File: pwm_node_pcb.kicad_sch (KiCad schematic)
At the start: 42 parts, among them J1 CAN1, J2 TC2050-IDC-NL, J3 Battery, J5 Load Source, J6 5V Breakout, U1 LMR51430, U2 TJA1051T/3, U3 LD1117S33CTR, U4 STM32L432KCU, U5 TXB0104QPWRQ1, Y1 ECS-2520MV-080-BN

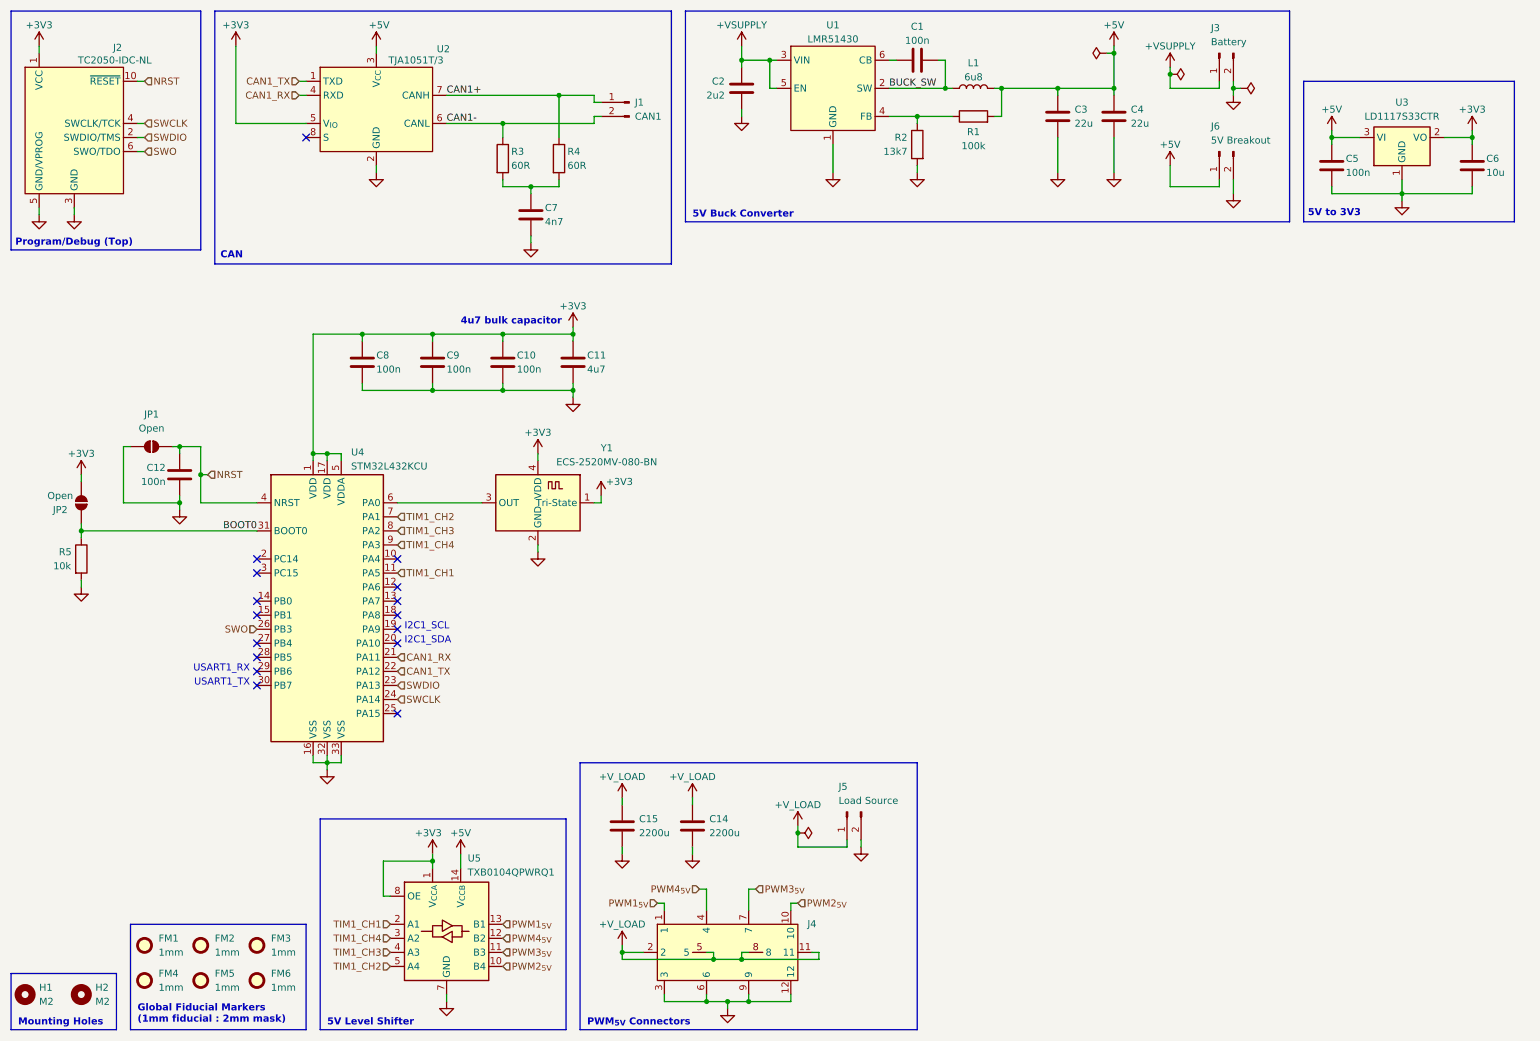
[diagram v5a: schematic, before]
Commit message: Add minor decoupling caps, board cleanup
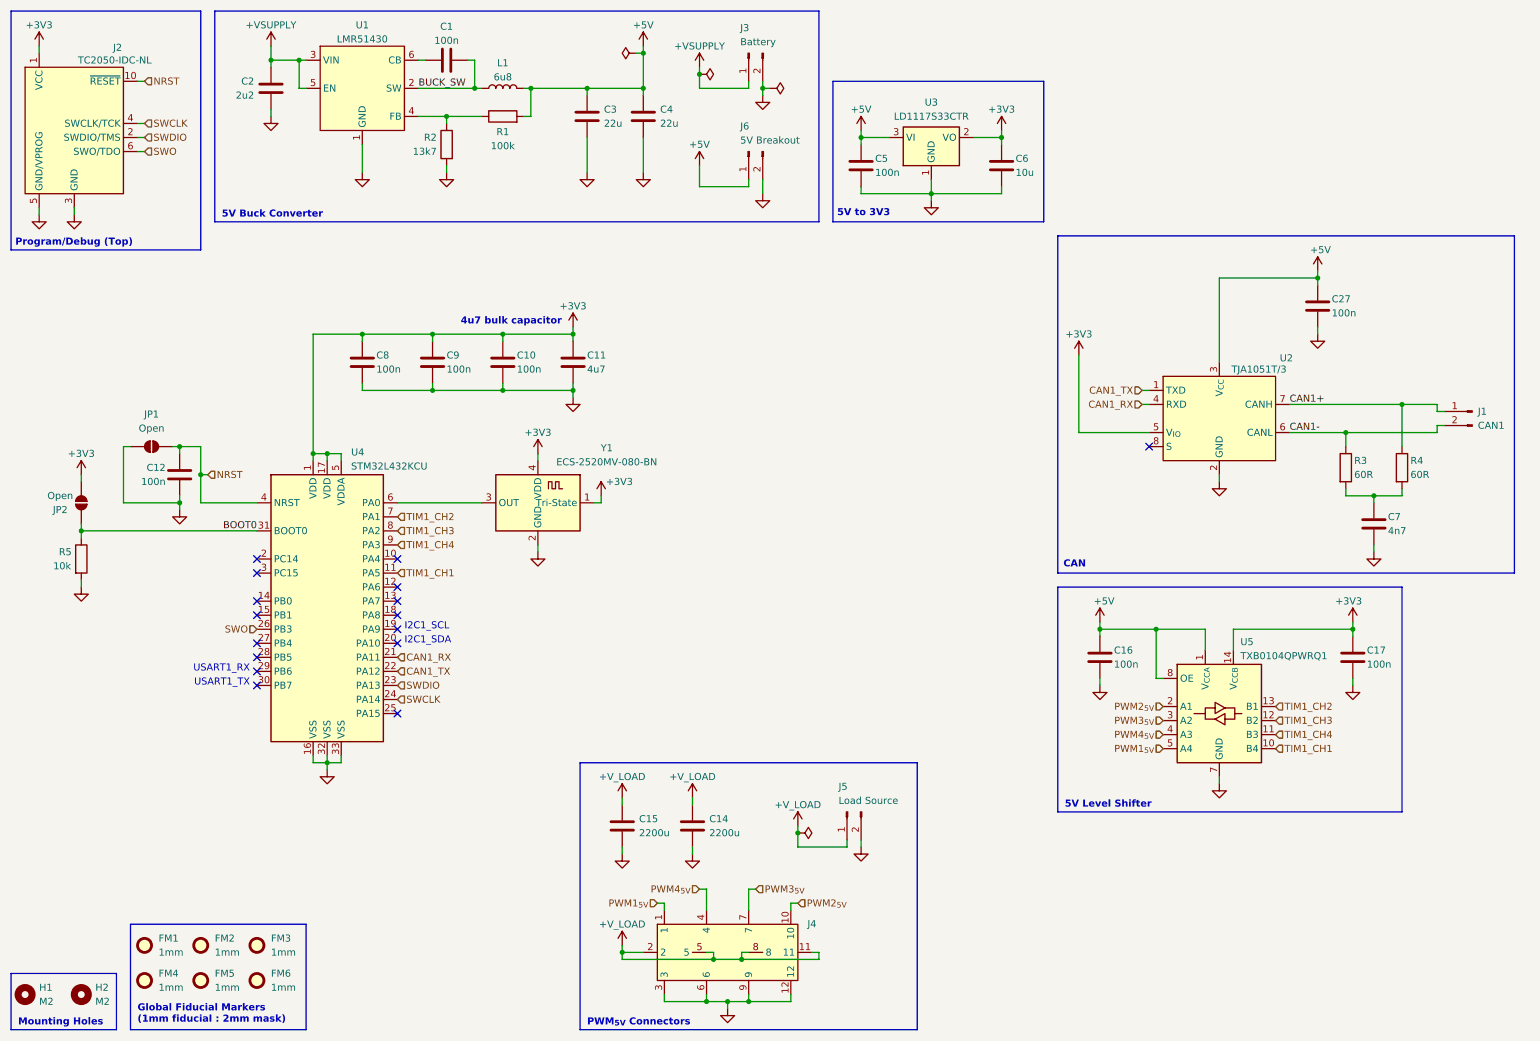
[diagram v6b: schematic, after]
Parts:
- added C16, C17, C27: 100n, Capacitor_SMD:C_0603_1608Metric, symbol Device:C
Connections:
- net +3V3: now also U5.14 (V_{CCB}), C17.1; no longer U5.1 (V_{CCA}), U5.8 (OE)
- net +5V: now also U5.1 (V_{CCA}), U5.8 (OE), C16.1, C27.1; no longer U5.14 (V_{CCB})
- net GND: now also C16.2, C17.2, C27.2
- net PWM1_{5V}: now also U5.5 (A4); no longer U5.13 (B1)
- net PWM2_{5V}: now also U5.2 (A1); no longer U5.10 (B4)
- net PWM3_{5V}: now also U5.3 (A2); no longer U5.11 (B3)
- net PWM4_{5V}: now also U5.4 (A3); no longer U5.12 (B2)
- net TIM1_CH1: now also U5.10 (B4); no longer U5.2 (A1)
- net TIM1_CH2: now also U5.13 (B1); no longer U5.5 (A4)
- net TIM1_CH3: now also U5.12 (B2); no longer U5.4 (A3)
- net TIM1_CH4: now also U5.11 (B3); no longer U5.3 (A2)
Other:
- moved on the sheet: C1, C2, C3, C4, C5, C6, C7, J1, J3, J6, L1, R1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

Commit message: Add TVS and schottky diodes
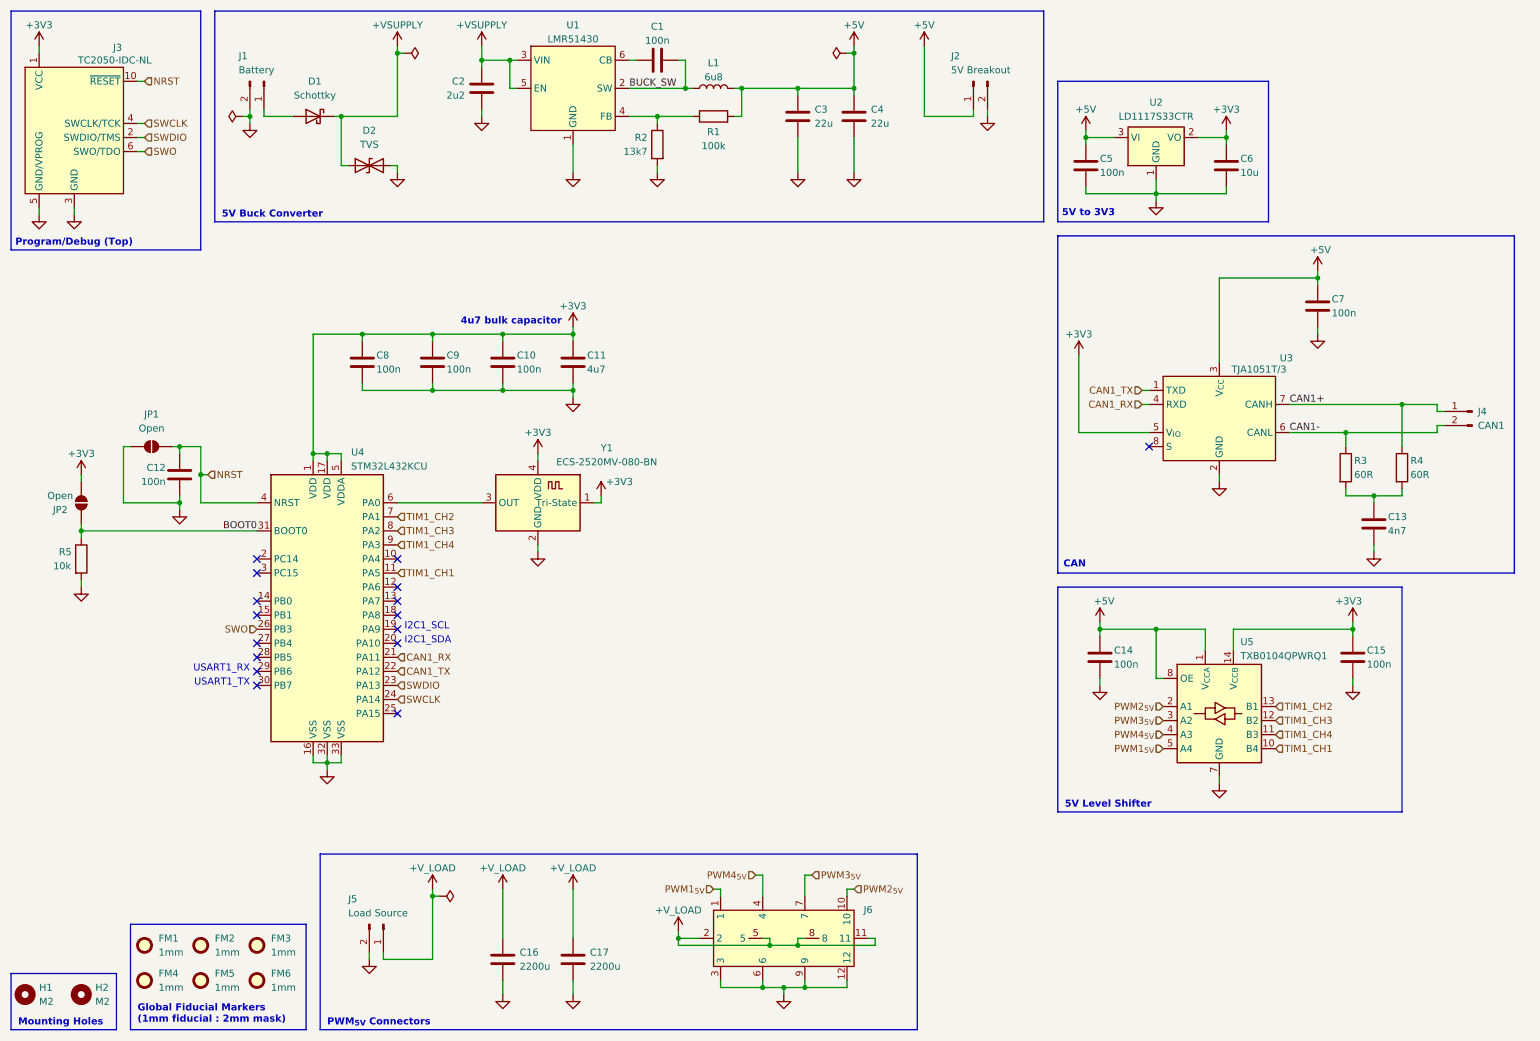
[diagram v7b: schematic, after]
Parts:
- added D1: Schottky, Diode_SMD:D_SMA, symbol Device:D_Schottky
- added D2: TVS, Diode_SMD:D_SMA, symbol Device:D_TVS
- renumbered C7 to C13, C16 to C14, C17 to C15, C15 to C16, C14 to C17, C27 to C7, J3 to J1, J6 to J2, J2 to J3, J1 to J4, J4 to J6, U3 to U2, U2 to U3
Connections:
- net +VSUPPLY: now also D1.1 (K), D2.1 (A1); no longer J1.1 (Pin_1)
- net GND: now also D2.2 (A2)
- new net: D1.2 (A), J1.1 (Pin_1)
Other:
- moved on the sheet: C1, C16, C17, C2, C3, C4, C5, C6, J1, J2, J5, J6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

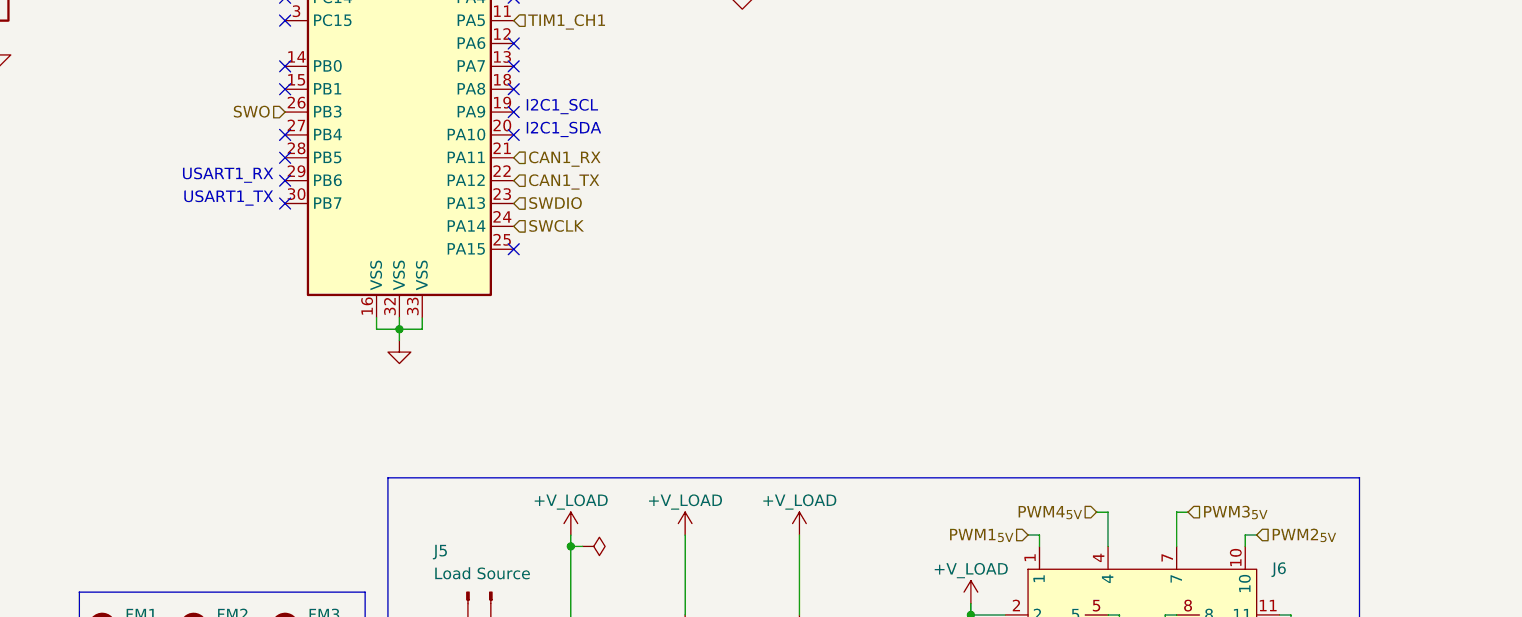
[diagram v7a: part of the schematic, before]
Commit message: Add testpads/UART breakout
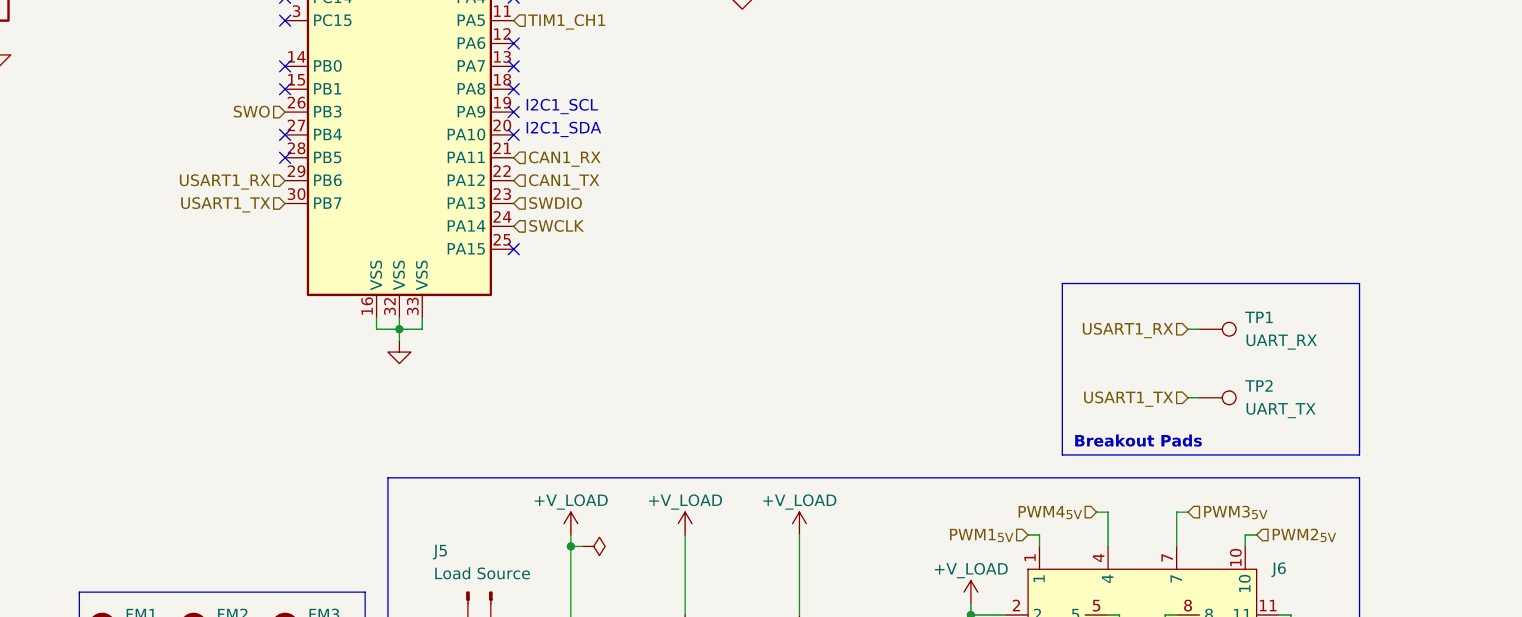
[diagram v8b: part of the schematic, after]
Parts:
- added TP1: UART_RX, TestPoint:TestPoint_Pad_D1.5mm, symbol Connector:TestPoint
- added TP2: UART_TX, TestPoint:TestPoint_Pad_D1.5mm, symbol Connector:TestPoint
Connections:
- net USART1_RX: now reaches U4.29 (PB6)
- net USART1_RX: now also TP1.1
- net USART1_TX: now reaches U4.30 (PB7)
- net USART1_TX: now also TP2.1
- no-connect marks 16 -> 14
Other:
- note added: "Breakout Pads"
- note removed: "USART1_RX"
- note removed: "USART1_TX"
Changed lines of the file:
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@@
 	)
 	(rectangle
+		(start 143.51 143.51)
+		(end 176.53 162.56)
+		(stroke
+			(width 0)
+			(type default)
+		)
+		(fill
+			(type none)
+		)
+	)
+	(rectangle
 		(start 34.29 177.8)
 		(end 66.04 196.85)
@@
 		)
 	)
-	(text "USART1_TX"
-		(exclude_from_sim no)
-		(at 55.88 134.112 0)
-		(effects
-			(font
-				(size 1.27 1.27)
-			)
-			(justify right)
-		)
-	)
 	(text "I2C1_SCL"
 		(exclude_from_sim no)
@@
 		)
 	)
-	(text "Global Fiducial Markers\n(1mm fiducial : 2mm mask)"
+	(text "I2C1_SDA"
 		(exclude_from_sim no)
-		(at 35.56 192.278 0)
+		(at 83.82 126.492 0)
+		(effects
+			(font
+				(size 1.27 1.27)
+			)
+			(justify left)
+		)
+	)
+	(text "Breakout Pads"
+		(exclude_from_sim no)
+		(at 144.78 160.528 0)
 		(effects
 			(font
@@
 		)
 	)
-	(text "Program/Debug (Top)"
+	(text "Global Fiducial Markers\n(1mm fiducial : 2mm mask)"
 		(exclude_from_sim no)
-		(at 13.462 53.848 0)
+		(at 35.56 192.278 0)
 		(effects
 			(font
@@
 		)
 	)
-	(text "I2C1_SDA"
+	(text "Program/Debug (Top)"
 		(exclude_from_sim no)
-		(at 83.82 126.492 0)
+		(at 13.462 53.848 0)
 		(effects
 			(font
 				(size 1.27 1.27)
+				(bold yes)
 			)
-			(justify left)
+			(justify left top)
 		)
 	)
@@
 		)
 	)
-	(text "USART1_RX"
-		(exclude_from_sim no)
-		(at 55.88 131.572 0)
-		(effects
-			(font
-				(size 1.27 1.27)
-			)
-			(justify right)
-		)
-	)
 	(junction
 		(at 232.41 35.56)
@@
 	)
 	(no_connect
+		(at 82.55 124.46)
+	)
+	(no_connect
 		(at 82.55 116.84)
 	)
@@
 	)
 	(no_connect
-		(at 57.15 114.3)
+		(at 82.55 127)
 	)
 	(no_connect
-		(at 82.55 127)
+		(at 57.15 114.3)
 	)
 	(no_connect
@@
 	)
 	(no_connect
-		(at 57.15 132.08)
-	)
-	(no_connect
 		(at 218.44 91.44)
 	)
 	(no_connect
-		(at 82.55 124.46)
-	)
-	(no_connect
 		(at 57.15 111.76)
 	)
@@
 		(at 57.15 129.54)
 	)
-	(no_connect
-		(at 57.15 134.62)
-	)
 	(wire
 		(pts
@@
 	(wire
 		(pts
+			(xy 157.48 156.21) (xy 158.75 156.21)
+		)
+		(stroke
+			(width 0)
+			(type default)
+		)
+	)
+	(wire
+		(pts
 			(xy 129.54 31.75) (xy 129.54 33.02)
 		)
@@
 	(wire
 		(pts
+			(xy 157.48 148.59) (xy 158.75 148.59)
+		)
+		(stroke
+			(width 0)
+			(type default)
+		)
+	)
+	(wire
+		(pts
 			(xy 80.01 184.15) (xy 80.01 182.88)
 		)
@@
 		)
 	)
+	(hierarchical_label "USART1_TX"
+		(shape input)
+		(at 157.48 156.21 180)
+		(effects
+			(font
+				(size 1.27 1.27)
+			)
+			(justify right)
+		)
+	)
 	(hierarchical_label "TIM1_CH2"
 		(shape input)
@@
 		)
 	)
+	(hierarchical_label "USART1_RX"
+		(shape input)
+		(at 157.48 148.59 180)
+		(effects
+			(font
+				(size 1.27 1.27)
+			)
+			(justify right)
+		)
+	)
 	(hierarchical_label "PWM1_{5V}"
 		(shape input)
@@
 		)
 	)
+	(hierarchical_label "USART1_TX"
+		(shape input)
+		(at 57.15 134.62 180)
+		(effects
+			(font
+				(size 1.27 1.27)
+			)
+			(justify right)
+		)
+	)
 	(hierarchical_label "SWDIO"
 		(shape input)
@@
 		)
 	)
+	(hierarchical_label "USART1_RX"
+		(shape input)
+		(at 57.15 132.08 180)
+		(effects
+			(font
+				(size 1.27 1.27)
+			)
+			(justify right)
+		)
+	)
 	(hierarchical_label "CAN1_RX"
 		(shape input)
@@
 	)
 	(symbol
+		(lib_id "Connector:TestPoint")
+		(at 158.75 156.21 270)
+		(unit 1)
+		(exclude_from_sim no)
+		(in_bom yes)
+		(on_board yes)
+		(dnp no)
+		(fields_autoplaced yes)
+		(property "Reference" "TP2"
+			(at 163.83 154.9399 90)
+			(effects
+				(font
+					(size 1.27 1.27)
+				)
+				(justify left)
+			)
+		)
+		(property "Value" "UART_TX"
+			(at 163.83 157.4799 90)
+			(effects
+				(font
+					(size 1.27 1.27)
+				)
+				(justify left)
+			)
+		)
+		(property "Footprint" "TestPoint:TestPoint_Pad_D1.5mm"
+			(at 158.75 161.29 0)
+			(effects
+				(font
+					(size 1.27 1.27)
+				)
+				(hide yes)
+			)
+		)
+		(property "Datasheet" "~"
+			(at 158.75 161.29 0)
+			(effects
+				(font
+					(size 1.27 1.27)
+				)
+				(hide yes)
+			)
+		)
+		(property "Description" "test point"
+			(at 158.75 156.21 0)
+			(effects
+				(font
+					(size 1.27 1.27)
+				)
+				(hide yes)
+			)
+		)
+		(pin "1"
+		)
+		(instances
+			(project "pwm_node_pcb"
+				(path "/5ad786da-b2c9-4f6e-bded-ab776aba6f67"
+					(reference "TP2")
+					(unit 1)
+				)
+			)
+		)
+	)
+	(symbol
 		(lib_id "power:+3V3")
 		(at 25.4 96.52 0)
@@
 					(unit 1)
 				)
+			)
+		)
+	)
+	(symbol
+		(lib_id "Connector:TestPoint")
+		(at 158.75 148.59 270)
+		(unit 1)
+		(exclude_from_sim no)
+		(in_bom yes)
+		(on_board yes)
+		(dnp no)
+		(fields_autoplaced yes)
+		(property "Reference" "TP1"
+			(at 163.83 147.3199 90)
+			(effects
+				(font
+					(size 1.27 1.27)
+				)
+				(justify left)
+			)
+		)
+		(property "Value" "UART_RX"
+			(at 163.83 149.8599 90)
+			(effects
+				(font
+					(size 1.27 1.27)
+				)
+				(justify left)
+			)
+		)
+		(property "Footprint" "TestPoint:TestPoint_Pad_D1.5mm"
+			(at 158.75 153.67 0)
+			(effects
+				(font
+					(size 1.27 1.27)
+				)
+				(hide yes)
+			)
+		)
+		(property "Datasheet" "~"
+			(at 158.75 153.67 0)
+			(effects
+				(font
+					(size 1.27 1.27)
+				)
+				(hide yes)
+			)
+		)
+		(property "Description" "test point"
+			(at 158.75 148.59 0)
+			(effects
+				(font
+					(size 1.27 1.27)
+				)
+				(hide yes)
+			)
+		)
+		(pin "1"
+		)
+		(instances
+			(project ""
+				(path "/5ad786da-b2c9-4f6e-bded-ab776aba6f67"
+					(reference "TP1")
+					(unit 1)
+				)
